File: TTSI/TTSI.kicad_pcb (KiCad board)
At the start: 2 copper layers, 6 parts, among them U101 74AHC1G32, U102 LM555xM, U103 74AHC1G08

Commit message: TSSI and FL fixes
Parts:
- added C101: 10uF, Capacitor_SMD:C_0402_1005Metric, F.Cu at (119.7, 28.6)
- added C102: 10uF, Capacitor_SMD:C_0402_1005Metric, F.Cu at (119.7, 30.6)
- added C105: 0.1u, Capacitor_SMD:C_0402_1005Metric, F.Cu at (119.7, 32.5)
- added C107: 0.1u, Capacitor_SMD:C_0402_1005Metric, F.Cu at (119.7, 34.5)
- added D101: D_TVS, Diode_SMD:D_SOD-123F, F.Cu at (78.8, 29.7)
- added D102: D_TVS, Diode_SMD:D_SOD-123F, F.Cu at (78.8, 33.0)
- added U103: R-78E5.0-0.5, Converter_DCDC:Converter_DCDC_RECOM_R-78E-0.5_THT, F.Cu at (109.2, 34.9)
- renumbered C102 to C103, C101 to C106, C103 to C108, U101 to U104, U103 to U106, U102 to U107
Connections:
- U106 pad 1: /CLOCK -> Net-(Q105-D)
- U106 pad 2: Net-(Q105-D) -> /CLOCK

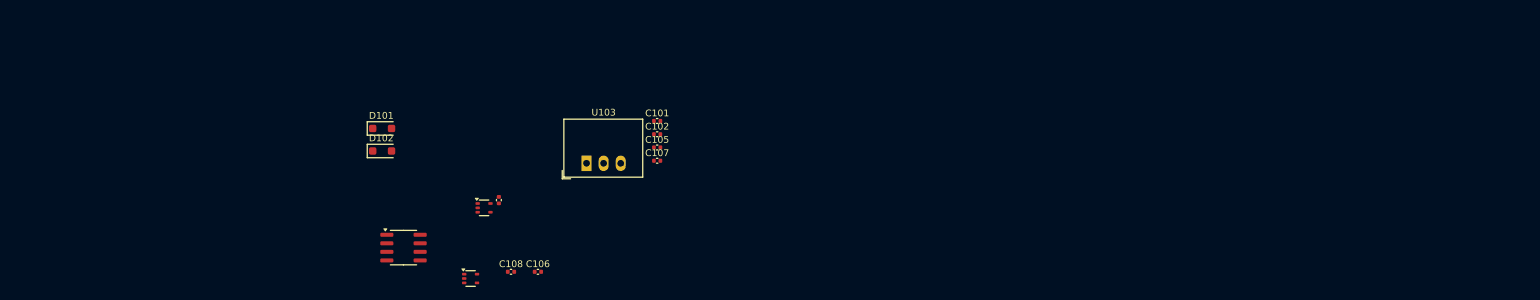
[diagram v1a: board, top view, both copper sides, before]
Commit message: Few changes to BOM as well as added 12v to bunny ears
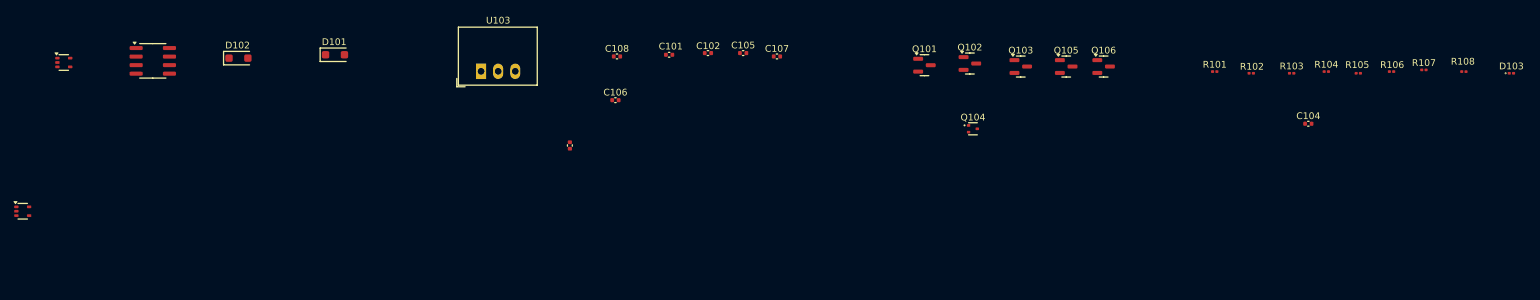
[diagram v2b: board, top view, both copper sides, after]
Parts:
- added C104: 1u, Capacitor_SMD:C_0402_1005Metric, F.Cu at (216.5, 29.0)
- added D103: RED, LED_SMD:LED_0201_0603Metric, F.Cu at (246.7, 21.5)
- added Q101: NMOS, Package_TO_SOT_SMD:SOT-23, F.Cu at (159.4, 20.3)
- added Q102: NMOS, Package_TO_SOT_SMD:SOT-23, F.Cu at (166.2, 20.1)
- added Q103: NMOS, Package_TO_SOT_SMD:SOT-23, F.Cu at (173.8, 20.5)
- added Q104: PMOS, Package_TO_SOT_SMD:SOT-523, F.Cu at (166.6, 29.8)
- added Q105: NMOS, Package_TO_SOT_SMD:SOT-23, F.Cu at (180.5, 20.5)
- added Q106: NMOS, Package_TO_SOT_SMD:SOT-23, F.Cu at (186.1, 20.5)
- added R101: 10k, Resistor_SMD:R_0201_0603Metric, F.Cu at (202.6, 21.2)
- added R102: 500R, Resistor_SMD:R_0201_0603Metric, F.Cu at (208.0, 21.5)
- added R103: 10k, Resistor_SMD:R_0201_0603Metric, F.Cu at (214.0, 21.5)
- added R104: 1k, Resistor_SMD:R_0201_0603Metric, F.Cu at (219.2, 21.2)
- added R105: 10k, Resistor_SMD:R_0201_0603Metric, F.Cu at (223.9, 21.5)
- added R106: 1k, Resistor_SMD:R_0201_0603Metric, F.Cu at (228.8, 21.2)
- added R107: R_US, Resistor_SMD:R_0201_0603Metric, F.Cu at (233.7, 21.0)
- added R108: 100k, Resistor_SMD:R_0201_0603Metric, F.Cu at (239.6, 21.2)
- moved U104 67.3 mm to (25.4, 42.0)
- moved U106 66.1 mm to (31.6, 19.9)
- moved U107 46.5 mm to (44.8, 19.7)
- moved C108 35.7 mm to (113.8, 19.0)
- moved C106 28.0 mm to (113.5, 25.5)
- moved D102 25.4 mm to (57.5, 19.2)
- moved C107 23.6 mm to (137.5, 19.0)
- moved U103 20.8 mm to (93.6, 21.2)
- moved C105 19.0 mm to (132.5, 18.5)
- moved C102 14.2 mm to (127.3, 18.5)
- moved C103 13.3 mm to (106.8, 32.2)
- moved D101 13.0 mm to (71.8, 18.8)
- moved C101 10.00 mm to (121.5, 18.8)

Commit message: R,C values for 555. Layout start
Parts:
- moved U106 154.6 mm to (167.5, 93.5), turned to 90 degrees
- moved U104 142.5 mm to (158.3, 93.5), turned to 90 degrees
- moved U107 125.8 mm to (147.0, 93.0)
- moved R107 116.5 mm to (146.7, 98.5)
- moved R108 113.0 mm to (152.0, 92.7), turned to 90 degrees
- moved C104 99.4 mm to (140.0, 92.5), turned to 90 degrees
- moved R104 93.8 mm to (160.5, 94.5), turned to -90 degrees
- moved R106 93.4 mm to (170.0, 93.8), turned to -90 degrees
- moved R105 92.3 mm to (165.5, 93.0), turned to -90 degrees
- moved C107 84.1 mm to (162.0, 99.5)
- moved C103 80.2 mm to (156.0, 95.5), turned to -90 degrees
- moved C106 79.0 mm to (152.0, 94.5), turned to 90 degrees
- moved Q105 77.3 mm to (163.6, 95.9), turned to -90 degrees
- moved C108 77.1 mm to (146.0, 89.0)
- moved U103 76.5 mm to (129.8, 88.6), turned to -90 degrees
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
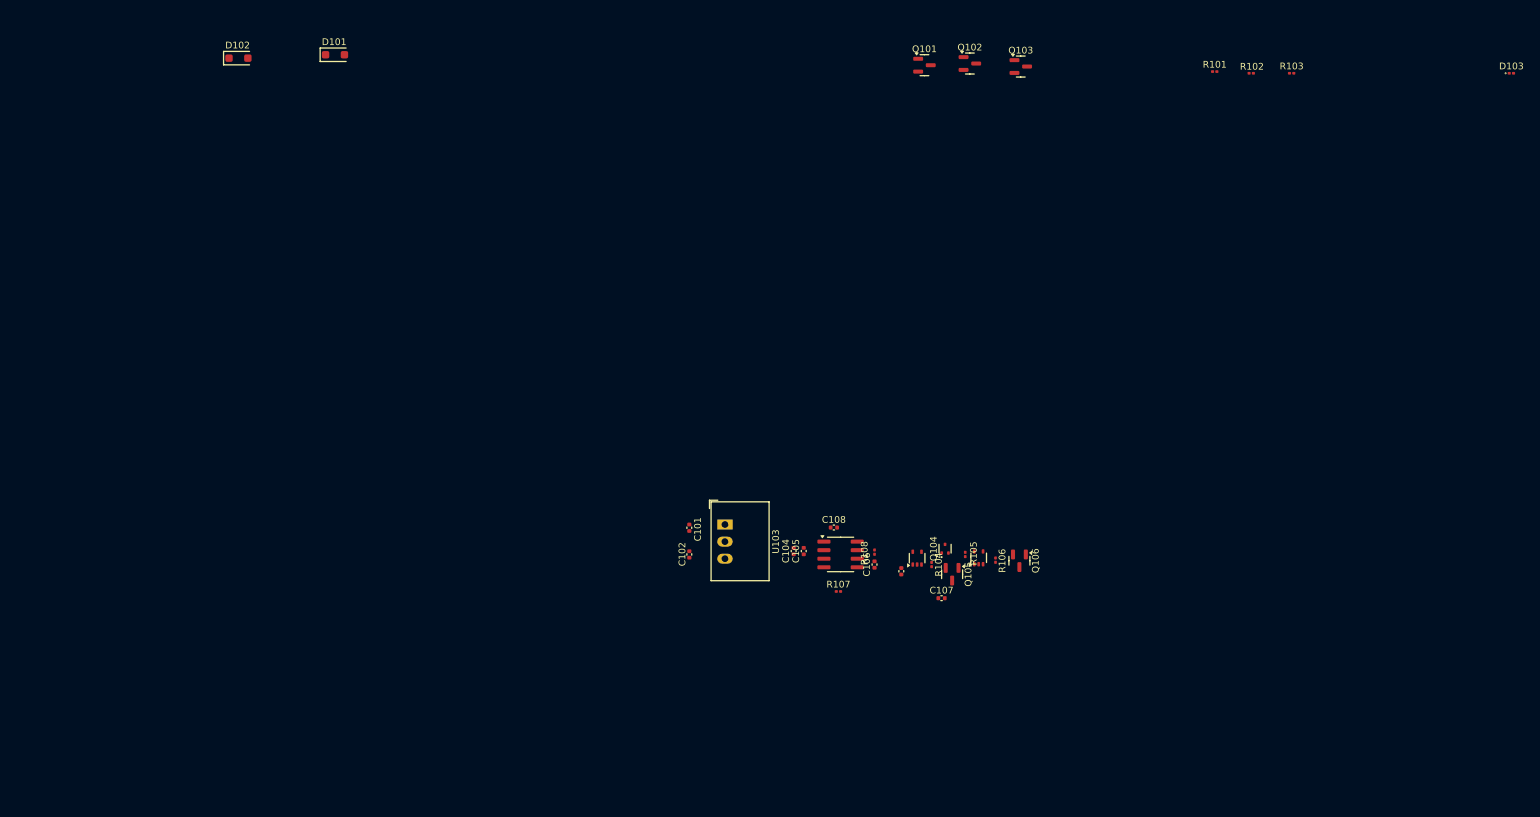
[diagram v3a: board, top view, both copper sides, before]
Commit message: Layout, routing, footprint addition, constraints set. Some component nets might be too small idk. But needs revision
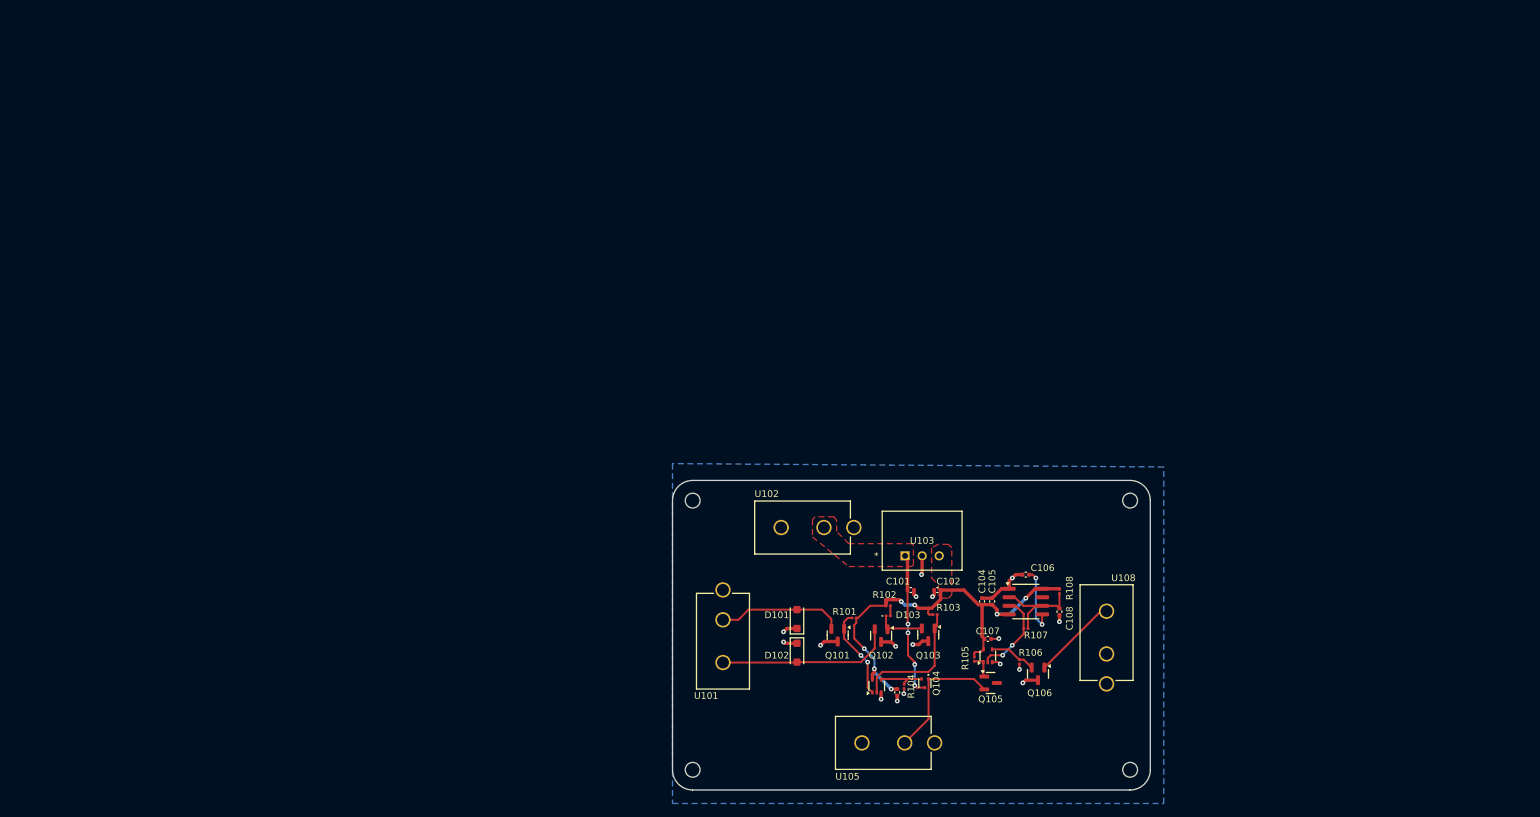
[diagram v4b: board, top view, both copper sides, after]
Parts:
- added H1: MountingHole, MountingHole:MountingHole_2.2mm_M2, F.Cu at (125.0, 85.0)
- added H2: MountingHole, MountingHole:MountingHole_2.2mm_M2, F.Cu at (125.0, 125.0)
- added H3: MountingHole, MountingHole:MountingHole_2.2mm_M2, F.Cu at (190.0, 125.0)
- added H4: MountingHole, MountingHole:MountingHole_2.2mm_M2, F.Cu at (190.0, 85.0)
- added U101: 641964-1, 641964-1:641964-1_TYC, F.Cu at (129.5, 102.7)
- added U102: 641964-1, 641964-1:641964-1_TYC, F.Cu at (144.5, 89.0)
- added U105: 641964-1, 641964-1:641964-1_TYC, F.Cu at (156.5, 121.0)
- added U108: 641964-1, 641964-1:641964-1_TYC, F.Cu at (186.5, 107.8)
- C108: value C -> 22u
- R107: value R_US -> 15k
- U103: footprint Converter_DCDC:Converter_DCDC_RECOM_R-78E-0.5_THT -> R_78E5_0_0_5 (1):R-78E-0.5_RCP
- moved D103 122.8 mm to (154.1, 102.1)
- moved D102 121.2 mm to (140.5, 107.6), turned to -90 degrees
- moved D101 108.4 mm to (140.5, 102.6), turned to 90 degrees
- moved R101 97.3 mm to (149.0, 102.4), turned to 180 degrees
- moved R103 96.3 mm to (161.0, 101.9)
- moved R102 95.8 mm to (154.1, 100.6)
- moved Q102 86.0 mm to (153.0, 105.1), turned to -90 degrees
- moved Q101 85.7 mm to (146.6, 105.0), turned to -90 degrees
- moved Q103 85.5 mm to (160.0, 104.9), turned to -90 degrees
- moved C102 37.2 mm to (161.4, 98.3), turned to 180 degrees
- moved C108 35.8 mm to (179.5, 101.5), turned to 90 degrees
- moved C101 34.2 mm to (157.4, 98.3), turned to 0 degrees
- moved C104 29.0 mm to (168.0, 100.0)
- moved C105 29.0 mm to (169.5, 100.0)
- moved U107 28.4 mm to (174.5, 100.0)
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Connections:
- Q104 pad 3: +5V -> +12V
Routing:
- net +5V: track 0.00 -> 65.8 mm, vias 0 -> 7
- net GND: track 0.00 -> 34.7 mm, vias 0 -> 17
- net IMD_HV: track 0.00 -> 26.3 mm
- net +12V: track 0.00 -> 21.5 mm, vias 0 -> 4
- net Net-(Q104-D): track 0.00 -> 20.0 mm
- net /IMD_LV: track 0.00 -> 19.3 mm
- net BMS_HV: track 0.00 -> 18.8 mm
- net /THRESH: track 0.00 -> 15.2 mm
- net /BMS_LV: track 0.00 -> 13.6 mm, vias 0 -> 2
- net /CLOCK: track 0.00 -> 13.1 mm, vias 0 -> 2
- net Net-(Q106-D): track 0.00 -> 12.7 mm
- net Net-(U107-CV): track 0.00 -> 10.0 mm, vias 0 -> 2
- net Net-(Q104-G): track 0.00 -> 9.08 mm
- net Net-(D103-K): track 0.00 -> 7.24 mm
- net Net-(Q106-G): track 0.00 -> 6.99 mm
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- added copper zone on F.Cu, net +12V
- added copper zone on F.Cu, net +5V
- added copper zone on B.Cu, net GND
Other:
- board outline added: 71 x 46 mm

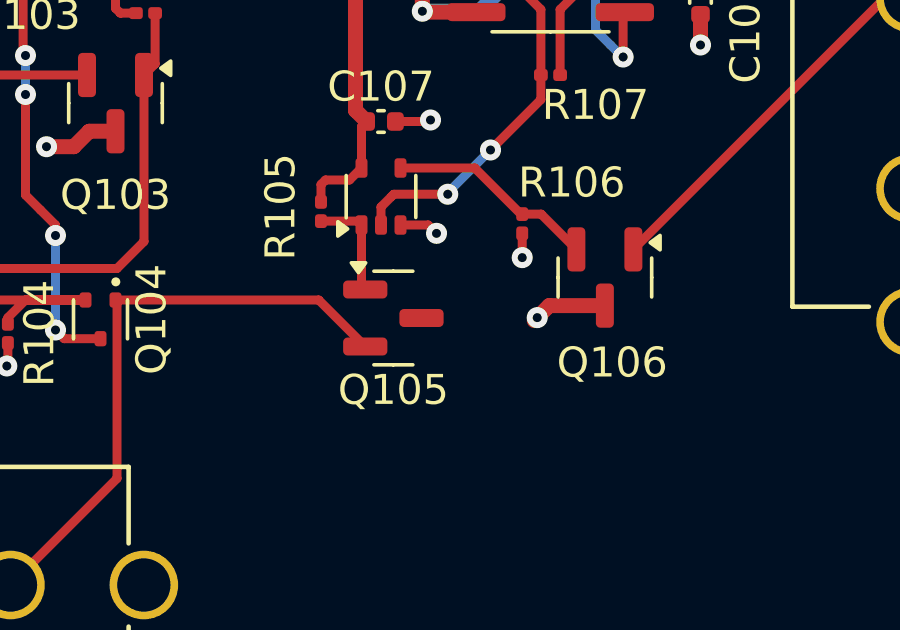
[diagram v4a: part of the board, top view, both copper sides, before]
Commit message: Redone logic for BSPD.
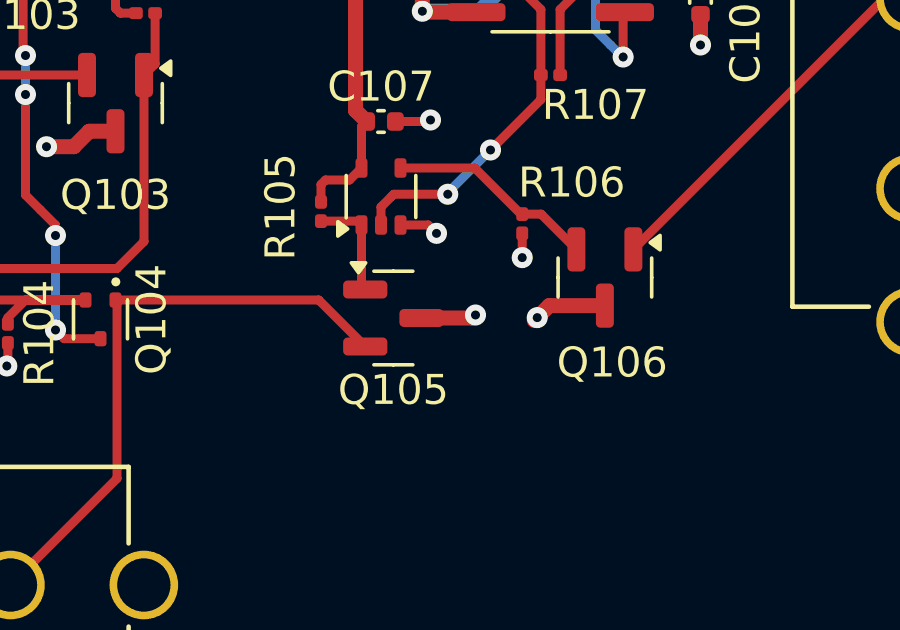
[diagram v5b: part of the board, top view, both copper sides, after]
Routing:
- net GND: track 34.7 -> 36.5 mm, vias 17 -> 18
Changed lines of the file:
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@@
 			)
 		)
-		(fp_text user "*"
-			(at -3.0099 0 0)
+		(fp_text user "${REFERENCE}"
+			(at 2.54 -2.249932 0)
 			(unlocked yes)
 			(layer "F.Fab")
@@
 			)
 		)
-		(fp_text user "${REFERENCE}"
-			(at 2.54 -2.249932 0)
+		(fp_text user "*"
+			(at -3.0099 0 0)
 			(unlocked yes)
 			(layer "F.Fab")
@@
 	)
 	(segment
+		(start 171.9 112.1)
+		(end 172 112)
+		(width 0.5)
+		(layer "F.Cu")
+		(net 3)
+	)
+	(segment
 		(start 157.88 98.9576)
 		(end 158.195589 99.273189)
@@
 		(net 3)
 	)
+	(segment
+		(start 170.2 112.1)
+		(end 171.9 112.1)
+		(width 0.5)
+		(layer "F.Cu")
+		(net 3)
+	)
 	(via
 		(at 179.5 103)
@@
 		(size 0.7)
 		(drill 0.3)
+		(layers "F.Cu" "B.Cu")
+		(net 3)
+	)
+	(via
+		(at 172 112)
+		(size 0.7)
+		(drill 0.3)

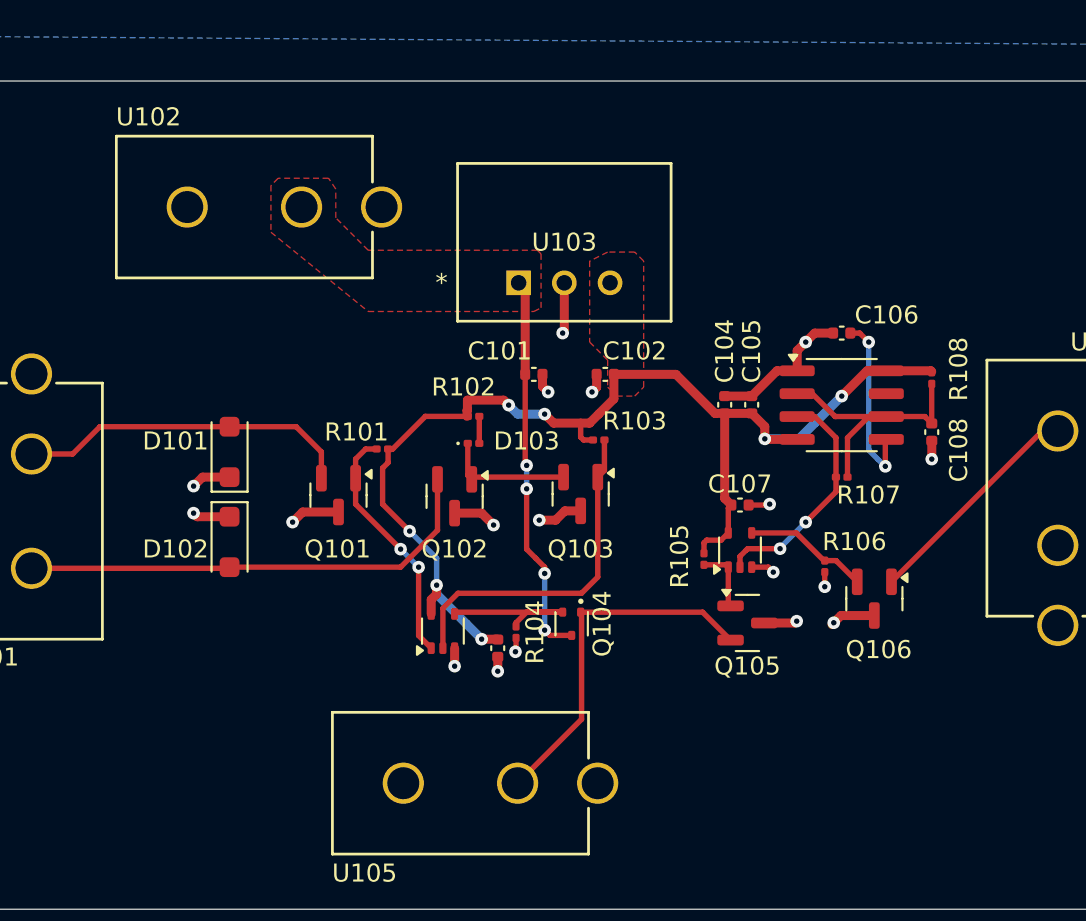
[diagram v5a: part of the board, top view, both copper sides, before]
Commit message: Fixed some errors on TSSI
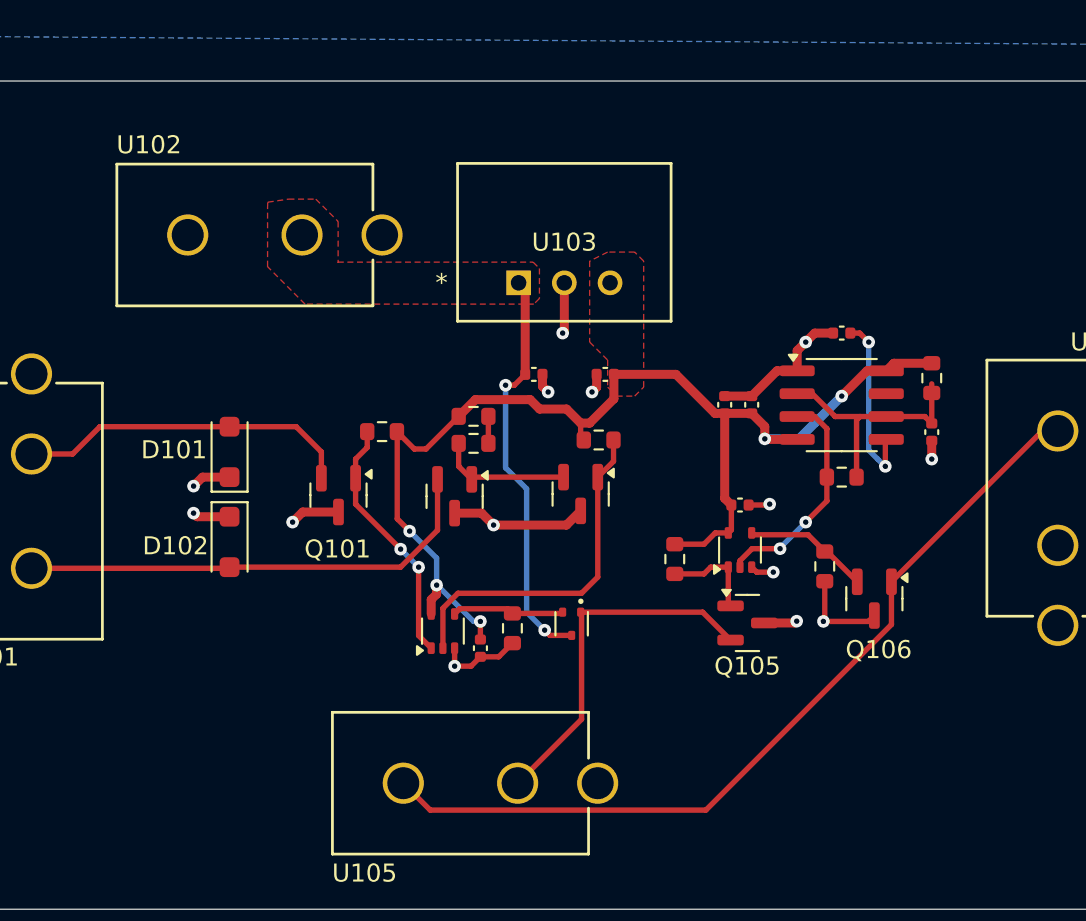
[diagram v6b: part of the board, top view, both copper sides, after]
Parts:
- D103: footprint LED_SMD:LED_0201_0603Metric -> Resistor_SMD:R_0603_1608Metric
- R101, R102, R103, R104, R105, R106, R107, R108: footprint Resistor_SMD:R_0201_0603Metric -> Resistor_SMD:R_0603_1608Metric
- moved R105 1.62 mm to (165.2, 108.5)
- moved U102 1.55 mm to (144.5, 90.6)
- moved R101 0.96 mm to (149.0, 101.5)
- moved C103 0.96 mm to (154.4, 113.5)
- moved R104 0.30 mm to (156.2, 112.4)
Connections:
- U105 pad 2: GND -> Net-(Q106-D)
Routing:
- net Net-(Q106-D): track 12.7 -> 47.1 mm
- net GND: track 36.5 -> 43.3 mm, vias 18 -> 14
- net Net-(Q104-G): track 9.08 -> 6.25 mm
- net Net-(Q105-D): track 3.61 -> 5.33 mm
- net /THRESH: track 15.2 -> 13.8 mm
- net +12V: track 21.5 -> 22.7 mm, vias 4 -> 2
- net /CLOCK: track 13.1 -> 12.5 mm
- net +5V: track 65.8 -> 65.7 mm, vias 7 -> 5
